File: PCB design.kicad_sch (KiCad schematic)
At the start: 19 parts

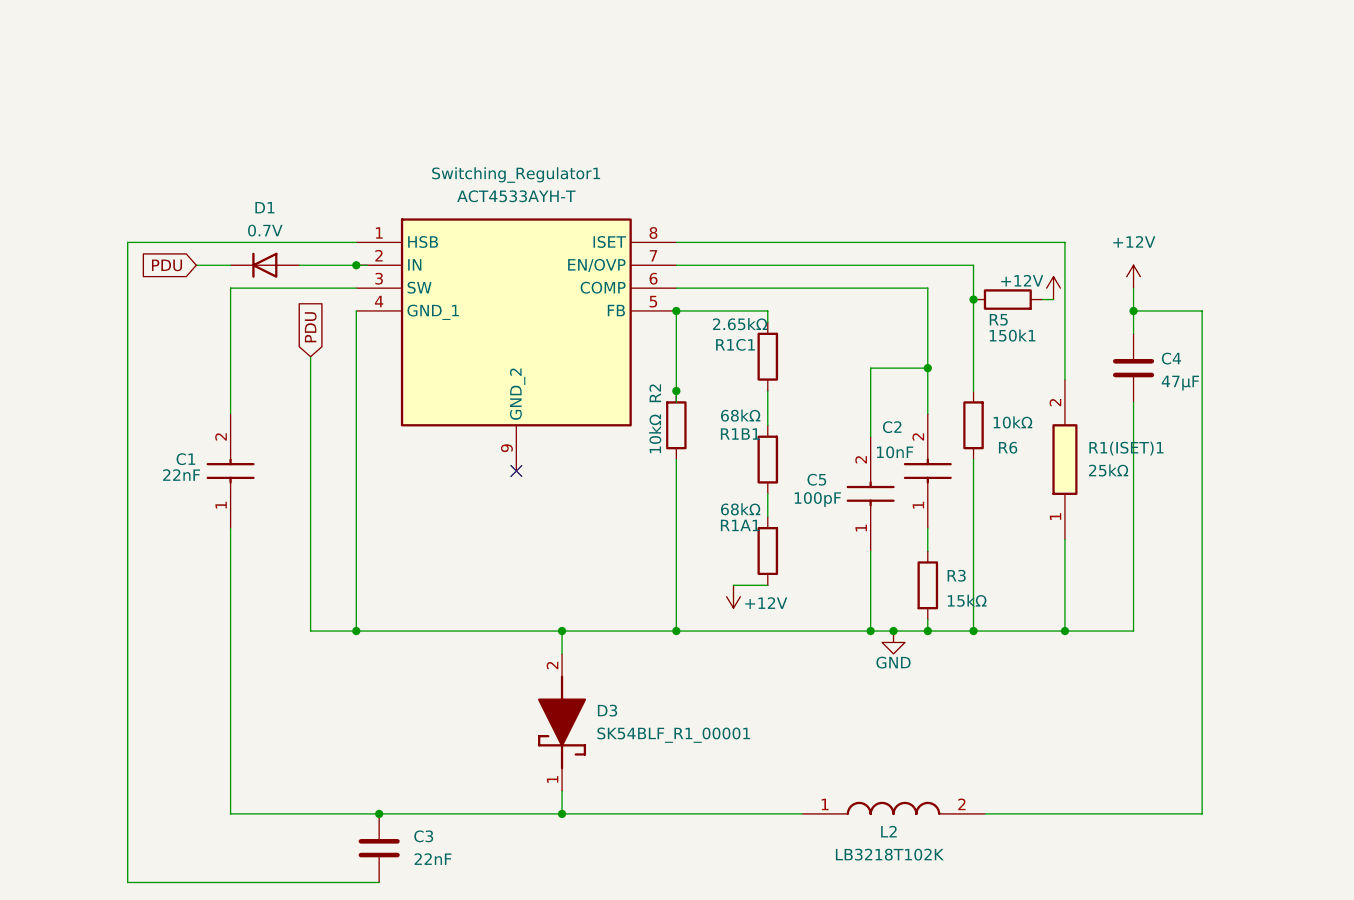
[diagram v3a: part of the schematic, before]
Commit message: Fixed annotations according to the datasheetinto the schematics
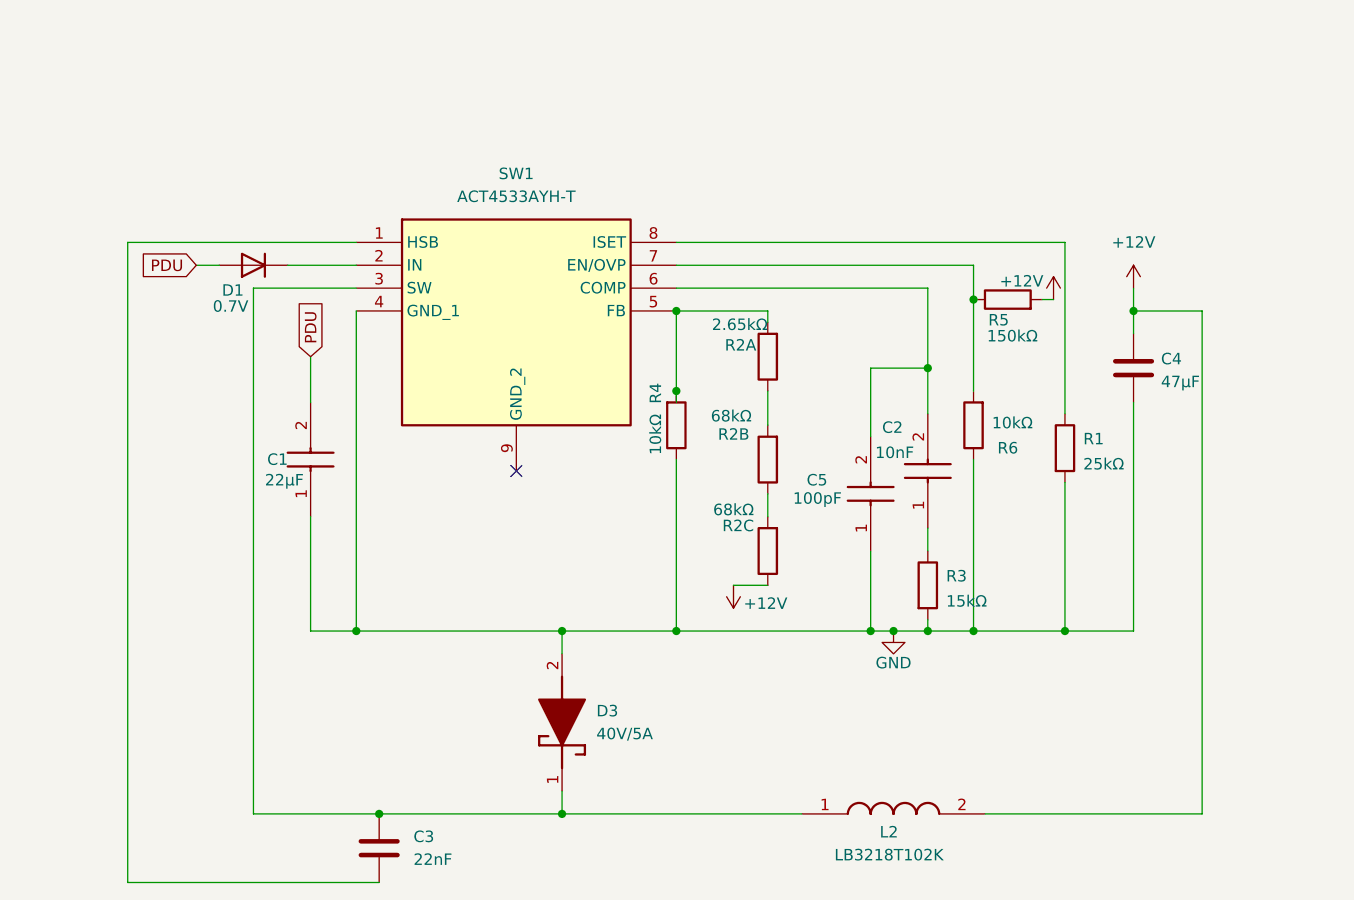
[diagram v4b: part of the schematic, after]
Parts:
- removed R1(ISET)1: 25kΩ, Resistor_SMD:R_01005_0402Metric_Pad0.57x0.30mm_HandSolder, symbol RN55E2502BRE6:RN55E2502BRE6
- added R1: 25kΩ, Resistor_SMD:R_1206_3216Metric_Pad1.30x1.75mm_HandSolder, symbol Device:R
- 150kΩ: renamed from 150k1; footprint Resistor_SMD:R_01005_0402Metric_Pad0.57x0.30mm_HandSolder -> Resistor_SMD:R_1206_3216Metric_Pad1.30x1.75mm_HandSolder
- C1: value 22nF -> 22µF; footprint Capacitor_SMD:C_01005_0402Metric_Pad0.57x0.30mm_HandSolder -> Capacitor_SMD:C_1812_4532Metric_Pad1.57x3.40mm_HandSolder
- C2: footprint Capacitor_SMD:C_01005_0402Metric_Pad0.57x0.30mm_HandSolder -> Capacitor_SMD:C_1206_3216Metric_Pad1.33x1.80mm_HandSolder
- D3: value SK54BLF_R1_00001 -> 40V/5A
- Female_Connector1: footprint Footprints:RESAD1526W69L610D229 -> Footprints:SFM-105-YY-XXX-D-A-K-TR
- R2A: renamed from R1C1; footprint Resistor_SMD:R_01005_0402Metric_Pad0.57x0.30mm_HandSolder -> Resistor_SMD:R_1206_3216Metric_Pad1.30x1.75mm_HandSolder
- R2B: renamed from R1B1; footprint Resistor_SMD:R_01005_0402Metric_Pad0.57x0.30mm_HandSolder -> Resistor_SMD:R_1206_3216Metric_Pad1.30x1.75mm_HandSolder
- R2C: renamed from R1A1; footprint Resistor_SMD:R_01005_0402Metric_Pad0.57x0.30mm_HandSolder -> Resistor_SMD:R_1206_3216Metric_Pad1.30x1.75mm_HandSolder
- R3, R6: footprint Resistor_SMD:R_01005_0402Metric_Pad0.57x0.30mm_HandSolder -> Resistor_SMD:R_1206_3216Metric_Pad1.30x1.75mm_HandSolder
- R4: renamed from R2; footprint Resistor_SMD:R_01005_0402Metric_Pad0.57x0.30mm_HandSolder -> Resistor_SMD:R_1206_3216Metric_Pad1.30x1.75mm_HandSolder
- renumbered Switching_Regulator1 to SW1
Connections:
- net GND: now also C1.1 (+), R1.2; no longer D1.1 (K), Male_Connector1.2
- net at C3.1, D3.1 (K), L2.1: now also SW1.3 (SW); no longer C1.1 (+)
- net at SW1.8 (ISET): now also R1.1
- net PDU: now reaches C1.2 (-)
- net PDU: now also D1.2 (A), Male_Connector1.2; no longer SW1.3 (SW)
- net at SW1.2 (IN): now also D1.1 (K); no longer D1.2 (A)

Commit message: Added all footprints to pcb design, something is fishy about the capasitors and resistances, we have too many resistors according to the datasheet and too few capasitors...
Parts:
- R5: renamed from 150kΩ; value R5 -> 150kΩ
- renumbered D1 to D0, D3 to D1, R2A to R2A1, R2B to R2B1, R2C to R2C1
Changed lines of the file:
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@@
 		(in_pos_files yes)
 		(dnp no)
-		(property "Reference" "150kΩ"
+		(property "Reference" "R5"
 			(at 189.738 80.264 90)
 			(show_name no)
@@
 			)
 		)
-		(property "Value" "R5"
-			(at 188.214 78.486 90)
+		(property "Value" "150kΩ"
+			(at 189.484 78.486 90)
 			(show_name no)
 			(do_not_autoplace no)
@@
 			(project "PCB design"
 				(path "/1ee13f0d-22f2-4352-9e68-759581f4b836"
-					(reference "150kΩ")
+					(reference "R5")
 					(unit 1)
 				)
@@
 		(in_pos_files yes)
 		(dnp no)
-		(property "Reference" "D1"
+		(property "Reference" "D0"
 			(at 103.124 75.184 0)
 			(show_name no)
@@
 			(project "PCB design"
 				(path "/1ee13f0d-22f2-4352-9e68-759581f4b836"
-					(reference "D1")
+					(reference "D0")
 					(unit 1)
 				)
@@
 		(dnp no)
 		(fields_autoplaced yes)
-		(property "Reference" "D3"
+		(property "Reference" "D1"
 			(at 143.51 121.9199 90)
 			(show_name no)
@@
 			(project "PCB design"
 				(path "/1ee13f0d-22f2-4352-9e68-759581f4b836"
-					(reference "D3")
+					(reference "D1")
 					(unit 1)
 				)
@@
 		(in_pos_files yes)
 		(dnp no)
-		(property "Reference" "R2C"
+		(property "Reference" "R2C1"
 			(at 161.036 101.346 0)
 			(show_name no)
@@
 			(project "PCB design"
 				(path "/1ee13f0d-22f2-4352-9e68-759581f4b836"
-					(reference "R2C")
+					(reference "R2C1")
 					(unit 1)
 				)
@@
 		(in_pos_files yes)
 		(dnp no)
-		(property "Reference" "R2A"
+		(property "Reference" "R2A1"
 			(at 161.29 81.28 0)
 			(show_name no)
@@
 			(project "PCB design"
 				(path "/1ee13f0d-22f2-4352-9e68-759581f4b836"
-					(reference "R2A")
+					(reference "R2A1")
 					(unit 1)
 				)
@@
 		(in_pos_files yes)
 		(dnp no)
-		(property "Reference" "R2B"
+		(property "Reference" "R2B1"
 			(at 160.528 91.186 0)
 			(show_name no)
@@
 			(project "PCB design"
 				(path "/1ee13f0d-22f2-4352-9e68-759581f4b836"
-					(reference "R2B")
+					(reference "R2B1")
 					(unit 1)
 				)

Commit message: Finished the ground layer and wiring of all components in PCB design. Ready for evaluation.
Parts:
- L2: value LB3218T102K -> 4.7µH
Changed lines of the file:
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@@
 			)
 		)
-		(property "Value" "LB3218T102K"
+		(property "Value" "4.7µH"
 			(at 176.022 137.922 0)
 			(show_name no)
